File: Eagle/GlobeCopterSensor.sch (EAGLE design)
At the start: 11 parts, among them IC1 MS5611-01BA03, U2 ADS1015

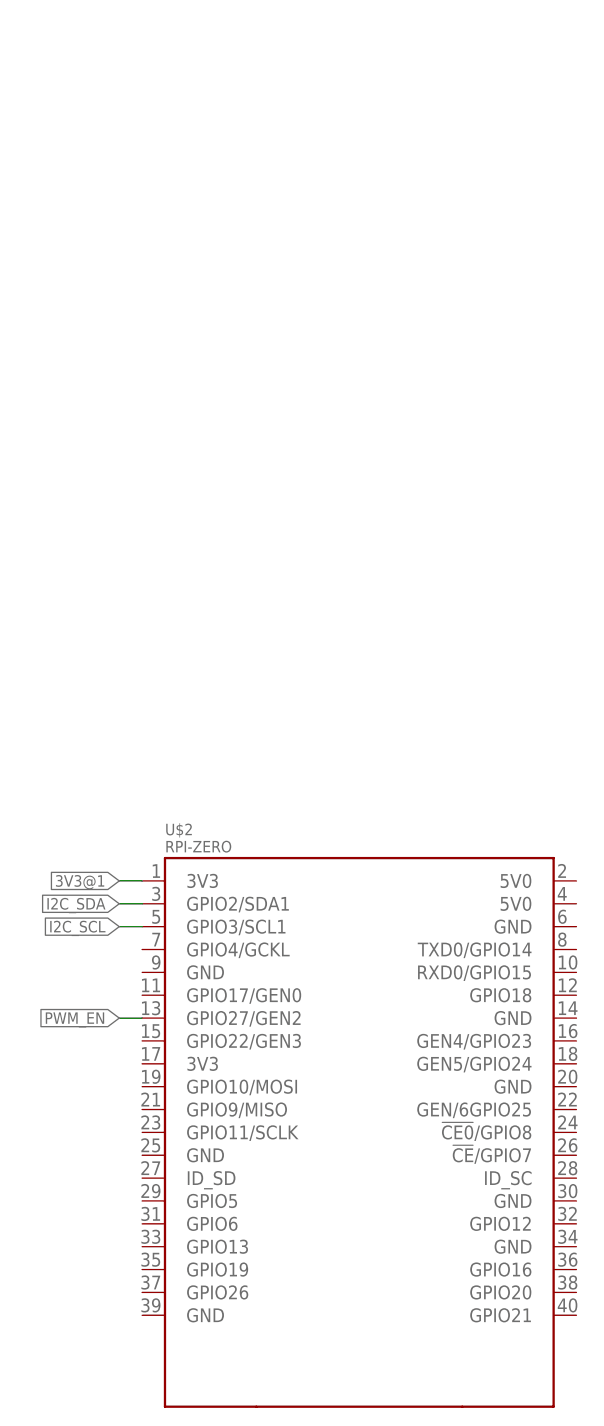
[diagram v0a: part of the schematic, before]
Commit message: remove unused 3.3v tag, connect rpi gnd, add i2c pullup part
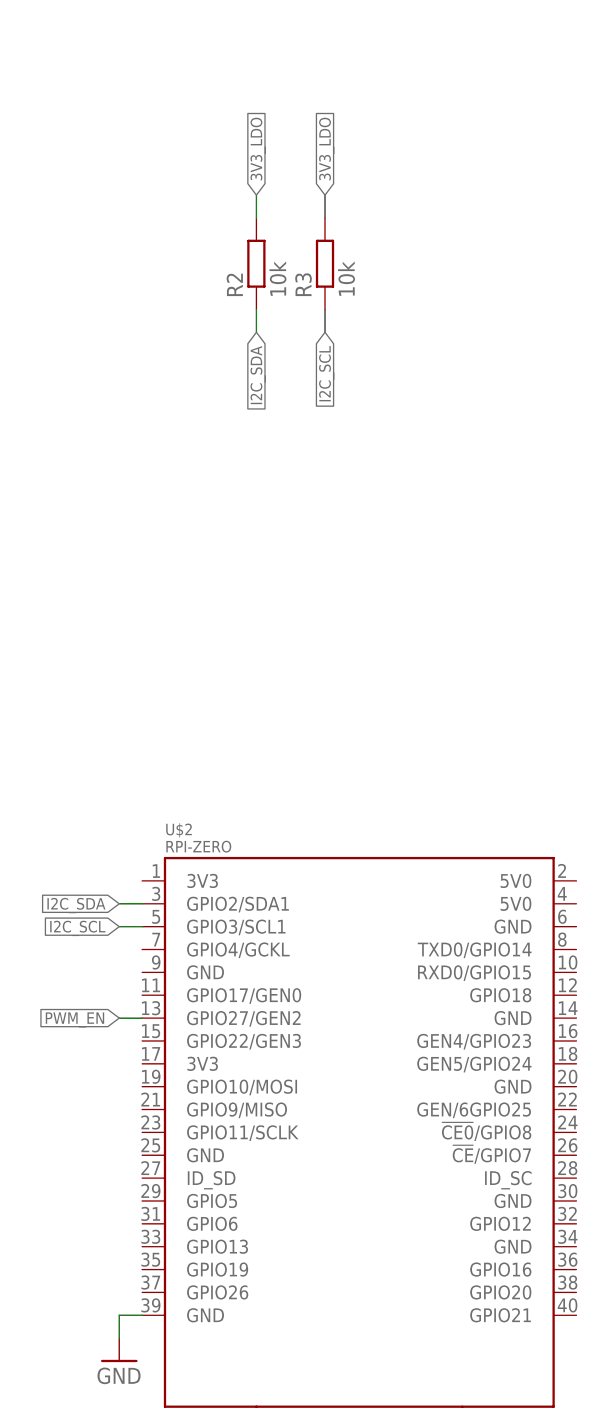
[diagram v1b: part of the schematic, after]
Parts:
- added R2, R3: 10k, resistor:R-EU_R0603
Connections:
- removed net 3V3@1: U$2.3V3@1
- net 3V3_LDO: now also R2.2, R3.2
- net GND: now also U$2.GND@3
- net I2C_SCL: now also R3.1
- net I2C_SDA: now also R2.1
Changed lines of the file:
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@@
 <part name="C5" library="resistor" library_urn="urn:adsk.eagle:library:348" deviceset="C-EU" device="C0603" value="10n"/>
 <part name="GND9" library="SparkFun-Aesthetics" deviceset="GND" device=""/>
+<part name="GND10" library="SparkFun-Aesthetics" deviceset="GND" device=""/>
+<part name="R2" library="resistor" library_urn="urn:adsk.eagle:library:348" deviceset="R-EU_" device="R0603" value="10k"/>
+<part name="R3" library="resistor" library_urn="urn:adsk.eagle:library:348" deviceset="R-EU_" device="R0603" value="10k"/>
 </parts>
 <sheets>
@@
 <instance part="C5" gate="G$1" x="137.16" y="66.04"/>
 <instance part="GND9" gate="1" x="137.16" y="58.42"/>
+<instance part="GND10" gate="1" x="43.18" y="48.26"/>
+<instance part="R2" gate="G$1" x="58.42" y="170.18" rot="R90"/>
+<instance part="R3" gate="G$1" x="66.04" y="170.18" rot="R90"/>
 </instances>
 <busses>
@@
 <label x="203.2" y="86.36" size="1.27" layer="95" xref="yes"/>
 </segment>
+<segment>
+<wire x1="58.42" y1="165.1" x2="58.42" y2="162.56" width="0.1524" layer="91"/>
+<label x="58.42" y="162.56" size="1.27" layer="95" rot="R270" xref="yes"/>
+<pinref part="R2" gate="G$1" pin="1"/>
+</segment>
 </net>
 <net name="I2C_SCL" class="0">
@@
 <label x="203.2" y="83.82" size="1.27" layer="95" xref="yes"/>
 </segment>
-</net>
-<net name="3V3@1" class="0">
-<segment>
-<pinref part="U$2" gate="G$1" pin="3V3@1"/>
-<wire x1="45.72" y1="101.6" x2="43.18" y2="101.6" width="0.1524" layer="91"/>
-<label x="43.18" y="101.6" size="1.27" layer="95" rot="R180" xref="yes"/>
+<segment>
+<wire x1="66.04" y1="165.1" x2="66.04" y2="162.56" width="0.1524" layer="91"/>
+<label x="66.04" y="162.56" size="1.27" layer="95" rot="R270" xref="yes"/>
+<pinref part="R3" gate="G$1" pin="1"/>
 </segment>
 </net>
@@
 <junction x="137.16" y="68.58"/>
 <label x="132.08" y="68.58" size="1.27" layer="95" rot="R180" xref="yes"/>
+</segment>
+<segment>
+<pinref part="R2" gate="G$1" pin="2"/>
+<wire x1="58.42" y1="175.26" x2="58.42" y2="177.8" width="0.1524" layer="91"/>
+<label x="58.42" y="177.8" size="1.27" layer="95" rot="R90" xref="yes"/>
+</segment>
+<segment>
+<pinref part="R3" gate="G$1" pin="2"/>
+<wire x1="66.04" y1="175.26" x2="66.04" y2="177.8" width="0.1524" layer="91"/>
+<label x="66.04" y="177.8" size="1.27" layer="95" rot="R90" xref="yes"/>
 </segment>
 </net>
@@
 <junction x="137.16" y="60.96"/>
 </segment>
-</net>
+<segment>
+<pinref part="U$2" gate="G$1" pin="GND@3"/>
+<wire x1="45.72" y1="53.34" x2="43.18" y2="53.34" width="0.1524" layer="91"/>
+<wire x1="43.18" y1="53.34" x2="43.18" y2="50.8" width="0.1524" layer="91"/>
+<pinref part="GND10" gate="1" pin="GND"/>
+</segment>
+</net>

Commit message: センサー部の基本的な設計完了　電源部等細部要調整
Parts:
- added 3V3_PIN, 5V0_PIN, GND_PIN, SCL_PIN, SDA_PIN: (no value), pinhead:PINHD-1X1
- added ADC_CON: BM04B-GHS-TBT, connector:BM04B-GHS-TBT
- added C6, C7: 0u1, resistor:C-EUC0603
- added F1: 1206L, ptc-littlefuse:1206L
- added R10, R11, R4, R5, R6, R7, R8, R9: 220, resistor:R-EU_R0603
- added SERVO_CON: PINHD-3X8, pinhead:PINHD-3X8
- C4: value 0u1 -> 2u2
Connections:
- removed net N$1: R1.1, U1.#OE
- new net !LED_AMBER!: U$2.GEN5/GPIO24
- new net !LED_BLUE!: U$2.GEN/6GPIO25
- new net 5V0: 5V0_PIN.1, C7.1, F1.1
- new net ADC0_IN: ADC_CON.3, U2.AIN0
- new net ADC1_IN: ADC_CON.4, U2.AIN1
- new net MPU9250_DRDY: U$1.INT
- new net MPU925_DRDY: U$2.GEN4/GPIO23
- new net N$3: F1.2, SERVO_CON.11, SERVO_CON.14, SERVO_CON.17, SERVO_CON.2, SERVO_CON.20, SERVO_CON.23, SERVO_CON.5, SERVO_CON.8
- new net PWM0_CON: R4.2, SERVO_CON.1
- new net PWM0_OUT: R4.1, U1.PWM0
- new net PWM1_CON: R5.2, SERVO_CON.4
- new net PWM1_OUT: R5.1, U1.PWM1
- new net PWM2_CON: R6.2, SERVO_CON.7
- new net PWM2_OUT: R6.1, U1.PWM2
- new net PWM3_CON: R7.2, SERVO_CON.10
- new net PWM3_OUT: R7.1, U1.PWM3
- new net PWM4_CON: R8.2, SERVO_CON.13
- new net PWM4_OUT: R8.1, U1.PWM4
- new net PWM5_CON: R9.2, SERVO_CON.16
- new net PWM5_OUT: R9.1, U1.PWM5
- new net PWM6_CON: R10.2, SERVO_CON.19
- new net PWM6_OUT: R10.1, U1.PWM6
- new net PWM7_CON: R11.2, SERVO_CON.22
- new net PWM7_OUT: R11.1, U1.PWM7
- net 3V3_LDO: now also 3V3_PIN.1, ADC_CON.1, C6.1, U$1.RESV
- net GND: now also ADC_CON.2, C6.2, C7.2, GND_PIN.1, SERVO_CON.12, SERVO_CON.15, SERVO_CON.18, SERVO_CON.21, SERVO_CON.24, SERVO_CON.3, SERVO_CON.6, SERVO_CON.9, U$1.FSYNC, U1.EXTCLK
- net I2C_SCL: now also SCL_PIN.1
- net I2C_SDA: now also SDA_PIN.1
- net PWM_EN: now also R1.1, U1.#OE
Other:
- moved on the sheet: C1, C4, C5, R1, R2, R3, U1, U2

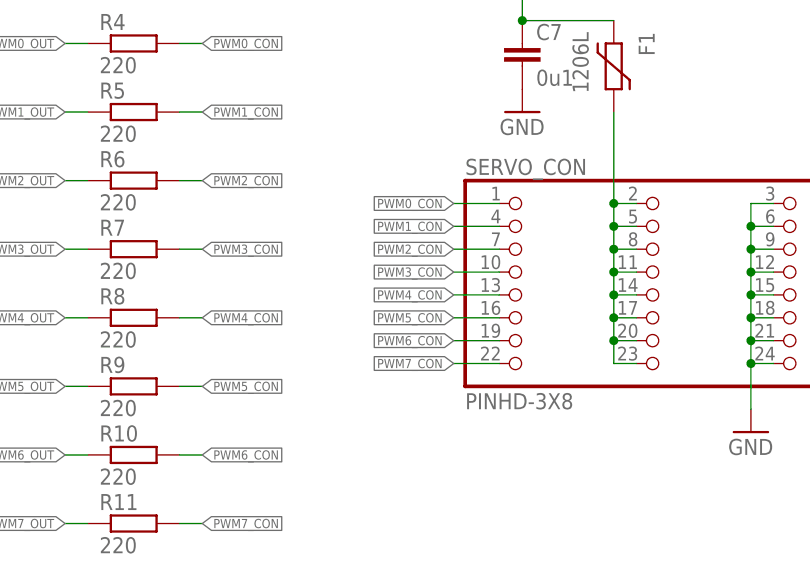
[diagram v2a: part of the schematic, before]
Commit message: 部品をすべて部品面に移動
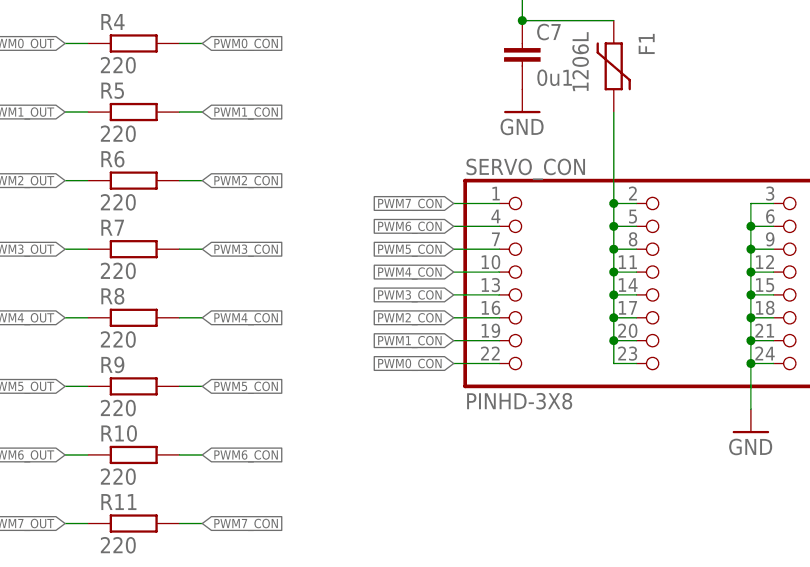
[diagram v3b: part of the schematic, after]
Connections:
- net PWM0_CON: now also SERVO_CON.22; no longer SERVO_CON.1
- net PWM1_CON: now also SERVO_CON.19; no longer SERVO_CON.4
- net PWM2_CON: now also SERVO_CON.16; no longer SERVO_CON.7
- net PWM3_CON: now also SERVO_CON.13; no longer SERVO_CON.10
- net PWM4_CON: now also SERVO_CON.10; no longer SERVO_CON.13
- net PWM5_CON: now also SERVO_CON.7; no longer SERVO_CON.16
- net PWM6_CON: now also SERVO_CON.4; no longer SERVO_CON.19
- net PWM7_CON: now also SERVO_CON.1; no longer SERVO_CON.22
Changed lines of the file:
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@@
 </segment>
 <segment>
-<pinref part="SERVO_CON" gate="G$1" pin="4"/>
-<wire x1="347.98" y1="165.1" x2="342.9" y2="165.1" width="0.1524" layer="91"/>
-<label x="342.9" y="165.1" size="1.016" layer="95" rot="R180" xref="yes"/>
+<pinref part="SERVO_CON" gate="G$1" pin="19"/>
+<wire x1="347.98" y1="152.4" x2="342.9" y2="152.4" width="0.1524" layer="91"/>
+<label x="342.9" y="152.4" size="1.016" layer="95" rot="R180" xref="yes"/>
 </segment>
 </net>
@@
 </segment>
 <segment>
-<pinref part="SERVO_CON" gate="G$1" pin="7"/>
-<wire x1="347.98" y1="162.56" x2="342.9" y2="162.56" width="0.1524" layer="91"/>
-<label x="342.9" y="162.56" size="1.016" layer="95" rot="R180" xref="yes"/>
+<pinref part="SERVO_CON" gate="G$1" pin="16"/>
+<wire x1="347.98" y1="154.94" x2="342.9" y2="154.94" width="0.1524" layer="91"/>
+<label x="342.9" y="154.94" size="1.016" layer="95" rot="R180" xref="yes"/>
 </segment>
 </net>
@@
 </segment>
 <segment>
-<pinref part="SERVO_CON" gate="G$1" pin="10"/>
-<wire x1="347.98" y1="160.02" x2="342.9" y2="160.02" width="0.1524" layer="91"/>
-<label x="342.9" y="160.02" size="1.016" layer="95" rot="R180" xref="yes"/>
+<pinref part="SERVO_CON" gate="G$1" pin="13"/>
+<wire x1="347.98" y1="157.48" x2="342.9" y2="157.48" width="0.1524" layer="91"/>
+<label x="342.9" y="157.48" size="1.016" layer="95" rot="R180" xref="yes"/>
 </segment>
 </net>
@@
 </segment>
 <segment>
-<pinref part="SERVO_CON" gate="G$1" pin="13"/>
-<wire x1="347.98" y1="157.48" x2="342.9" y2="157.48" width="0.1524" layer="91"/>
-<label x="342.9" y="157.48" size="1.016" layer="95" rot="R180" xref="yes"/>
+<pinref part="SERVO_CON" gate="G$1" pin="10"/>
+<wire x1="347.98" y1="160.02" x2="342.9" y2="160.02" width="0.1524" layer="91"/>
+<label x="342.9" y="160.02" size="1.016" layer="95" rot="R180" xref="yes"/>
 </segment>
 </net>
@@
 </segment>
 <segment>
-<pinref part="SERVO_CON" gate="G$1" pin="16"/>
-<wire x1="347.98" y1="154.94" x2="342.9" y2="154.94" width="0.1524" layer="91"/>
-<label x="342.9" y="154.94" size="1.016" layer="95" rot="R180" xref="yes"/>
+<pinref part="SERVO_CON" gate="G$1" pin="7"/>
+<wire x1="347.98" y1="162.56" x2="342.9" y2="162.56" width="0.1524" layer="91"/>
+<label x="342.9" y="162.56" size="1.016" layer="95" rot="R180" xref="yes"/>
 </segment>
 </net>
@@
 </segment>
 <segment>
-<pinref part="SERVO_CON" gate="G$1" pin="19"/>
-<wire x1="347.98" y1="152.4" x2="342.9" y2="152.4" width="0.1524" layer="91"/>
-<label x="342.9" y="152.4" size="1.016" layer="95" rot="R180" xref="yes"/>
+<pinref part="SERVO_CON" gate="G$1" pin="4"/>
+<wire x1="347.98" y1="165.1" x2="342.9" y2="165.1" width="0.1524" layer="91"/>
+<label x="342.9" y="165.1" size="1.016" layer="95" rot="R180" xref="yes"/>
 </segment>
 </net>
@@
 </segment>
 <segment>
-<pinref part="SERVO_CON" gate="G$1" pin="22"/>
-<wire x1="347.98" y1="149.86" x2="342.9" y2="149.86" width="0.1524" layer="91"/>
-<label x="342.9" y="149.86" size="1.016" layer="95" rot="R180" xref="yes"/>
+<pinref part="SERVO_CON" gate="G$1" pin="1"/>
+<wire x1="347.98" y1="167.64" x2="342.9" y2="167.64" width="0.1524" layer="91"/>
+<label x="342.9" y="167.64" size="1.016" layer="95" rot="R180" xref="yes"/>
 </segment>
 </net>
@@
 </segment>
 <segment>
-<pinref part="SERVO_CON" gate="G$1" pin="1"/>
-<wire x1="347.98" y1="167.64" x2="342.9" y2="167.64" width="0.1524" layer="91"/>
-<label x="342.9" y="167.64" size="1.016" layer="95" rot="R180" xref="yes"/>
+<pinref part="SERVO_CON" gate="G$1" pin="22"/>
+<wire x1="347.98" y1="149.86" x2="342.9" y2="149.86" width="0.1524" layer="91"/>
+<label x="342.9" y="149.86" size="1.016" layer="95" rot="R180" xref="yes"/>
 </segment>
 </net>
